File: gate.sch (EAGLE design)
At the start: 25 parts, among them IC1 MAX3232CSE, IC2 LM386M-1, J1 RJ11-2X, X1 MINI-USB-SCHIELD-32005-301

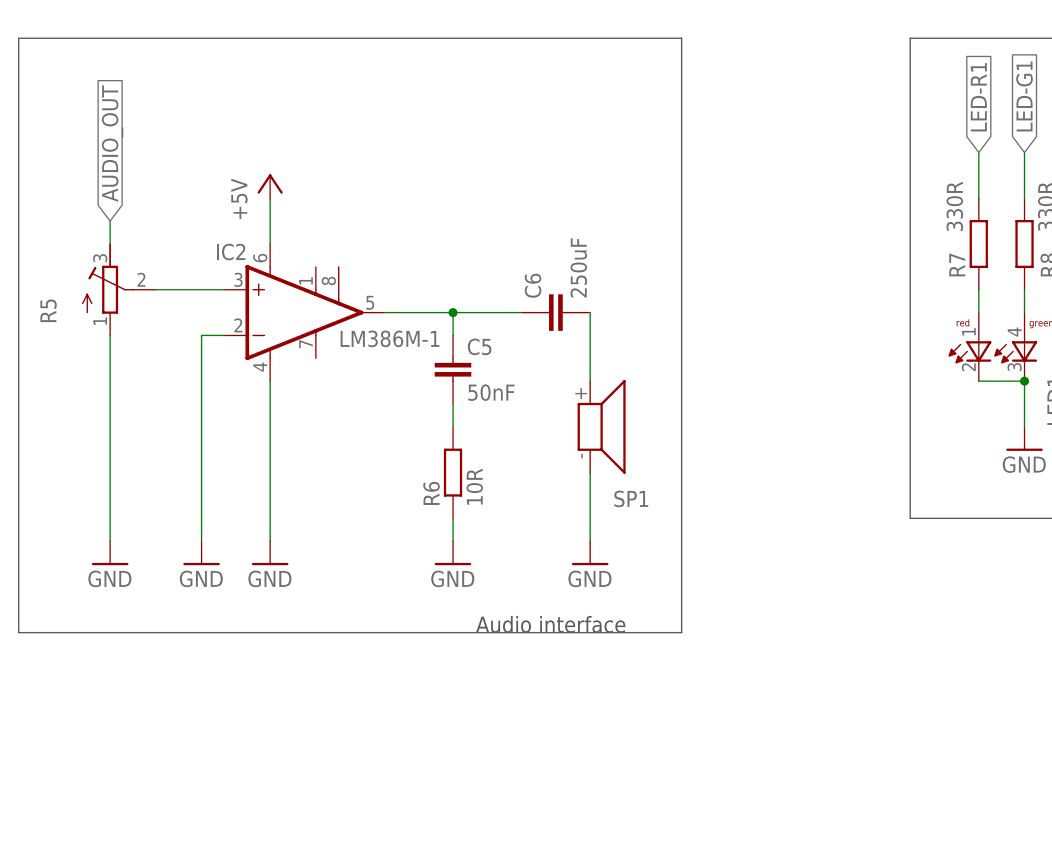
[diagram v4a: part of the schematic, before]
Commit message: Add volume resistor ladder for audio output
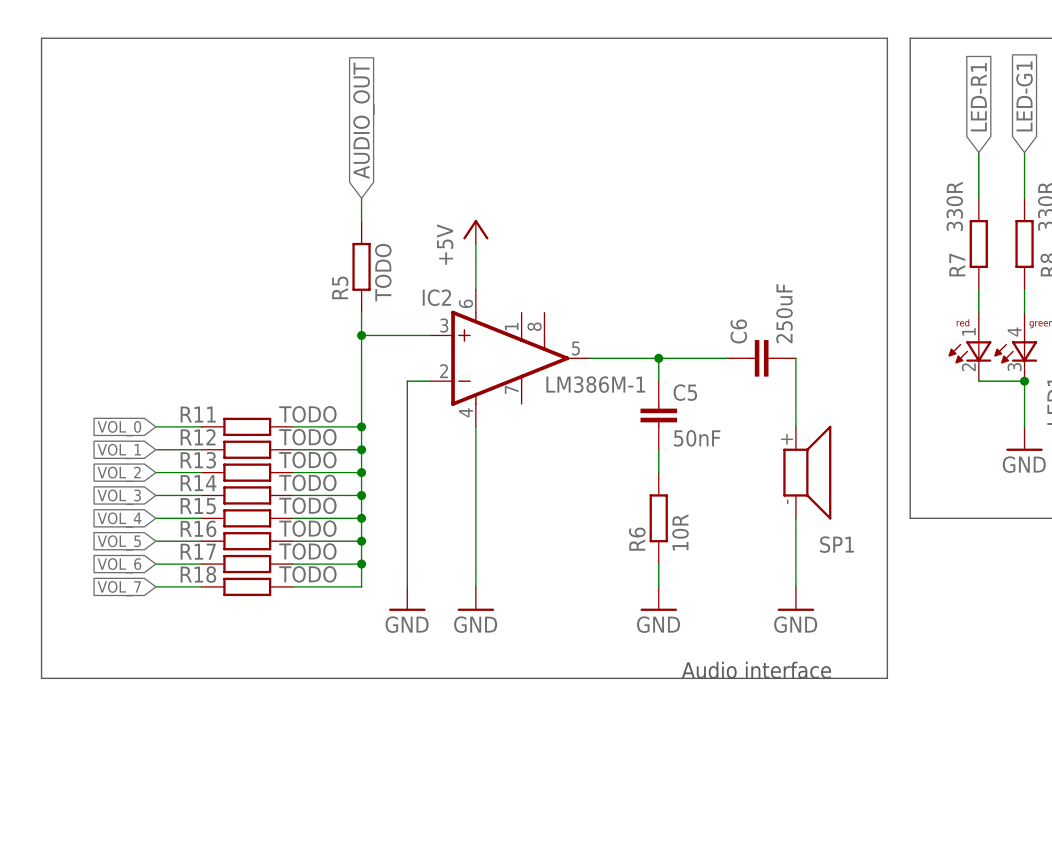
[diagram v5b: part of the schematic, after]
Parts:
- added R11, R12, R13, R14, R15, R16, R17, R18: TODO, rcl:R-EU_R0805
- R5: value (none) -> TODO; device rcl:R-TRIMM3339P -> rcl:R-EU_R0805
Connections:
- new net VOL_0: R11.1
- new net VOL_1: R12.1
- new net VOL_2: R13.1
- new net VOL_3: R14.1
- new net VOL_4: R15.1
- new net VOL_5: R16.1
- new net VOL_6: R17.1
- new net VOL_7: R18.1
- net AUDIO_OUT: now also R5.2; no longer R5.E
- net GND: no longer R5.A
- net N$15: now also R11.2, R12.2, R13.2, R14.2, R15.2, R16.2, R17.2, R18.2, R5.1; no longer R5.S
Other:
- moved on the sheet: C5, C6, IC2, R6, SP1

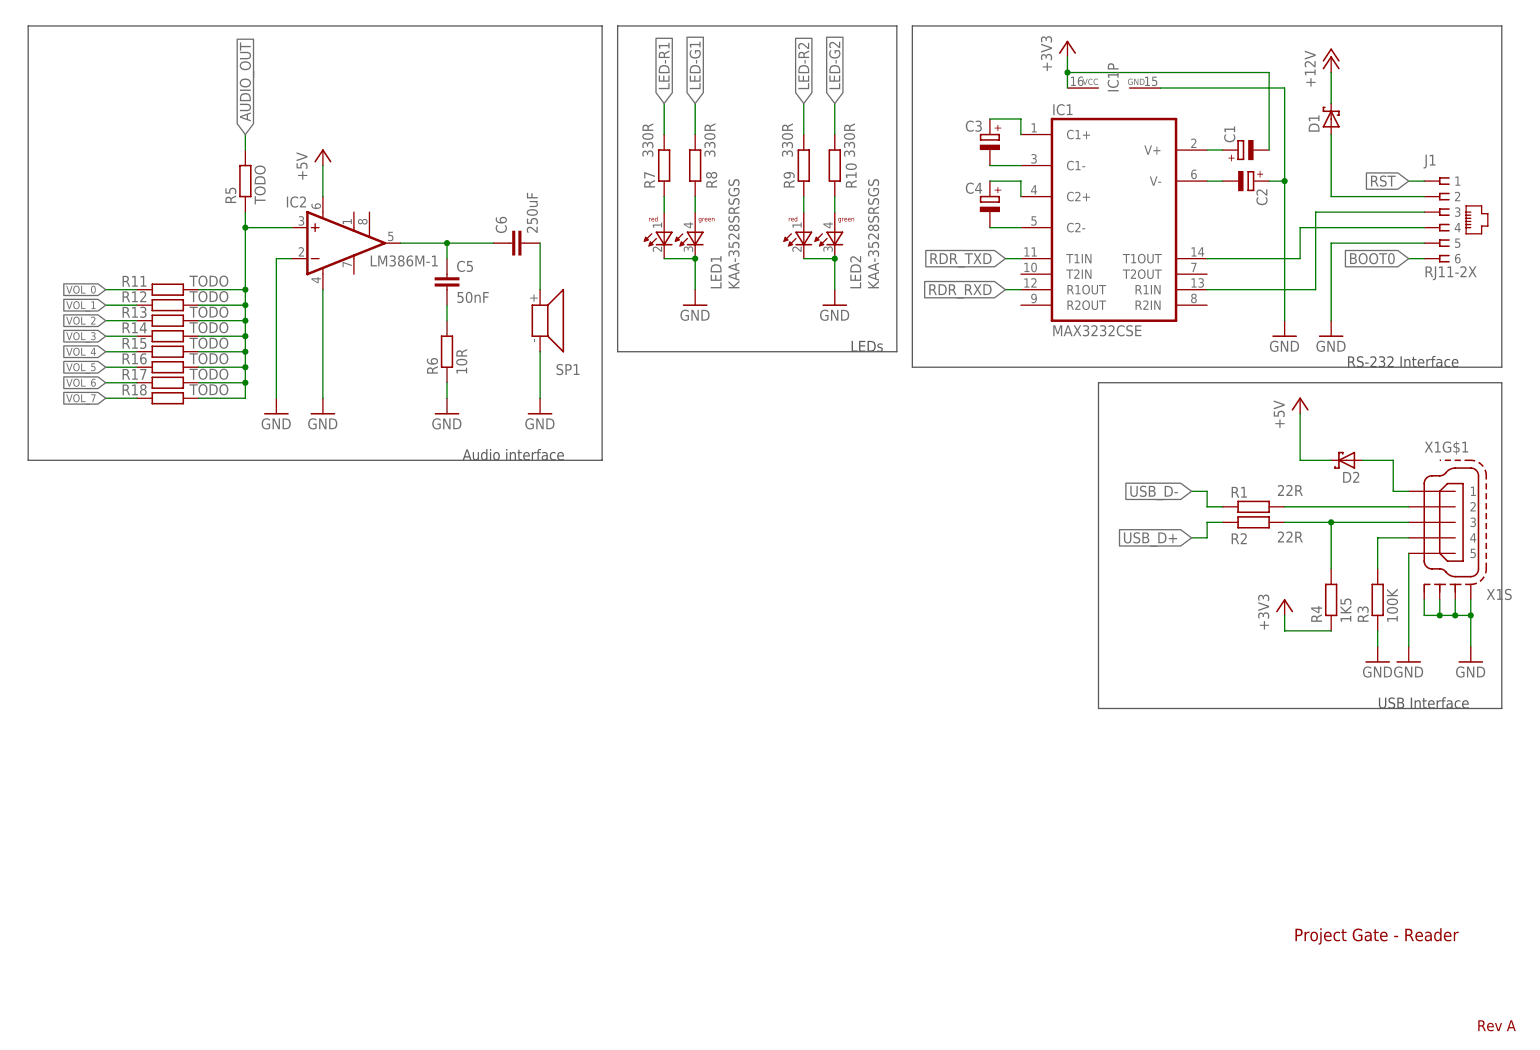
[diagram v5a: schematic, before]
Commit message: Add STM32F0[72|51] MCU
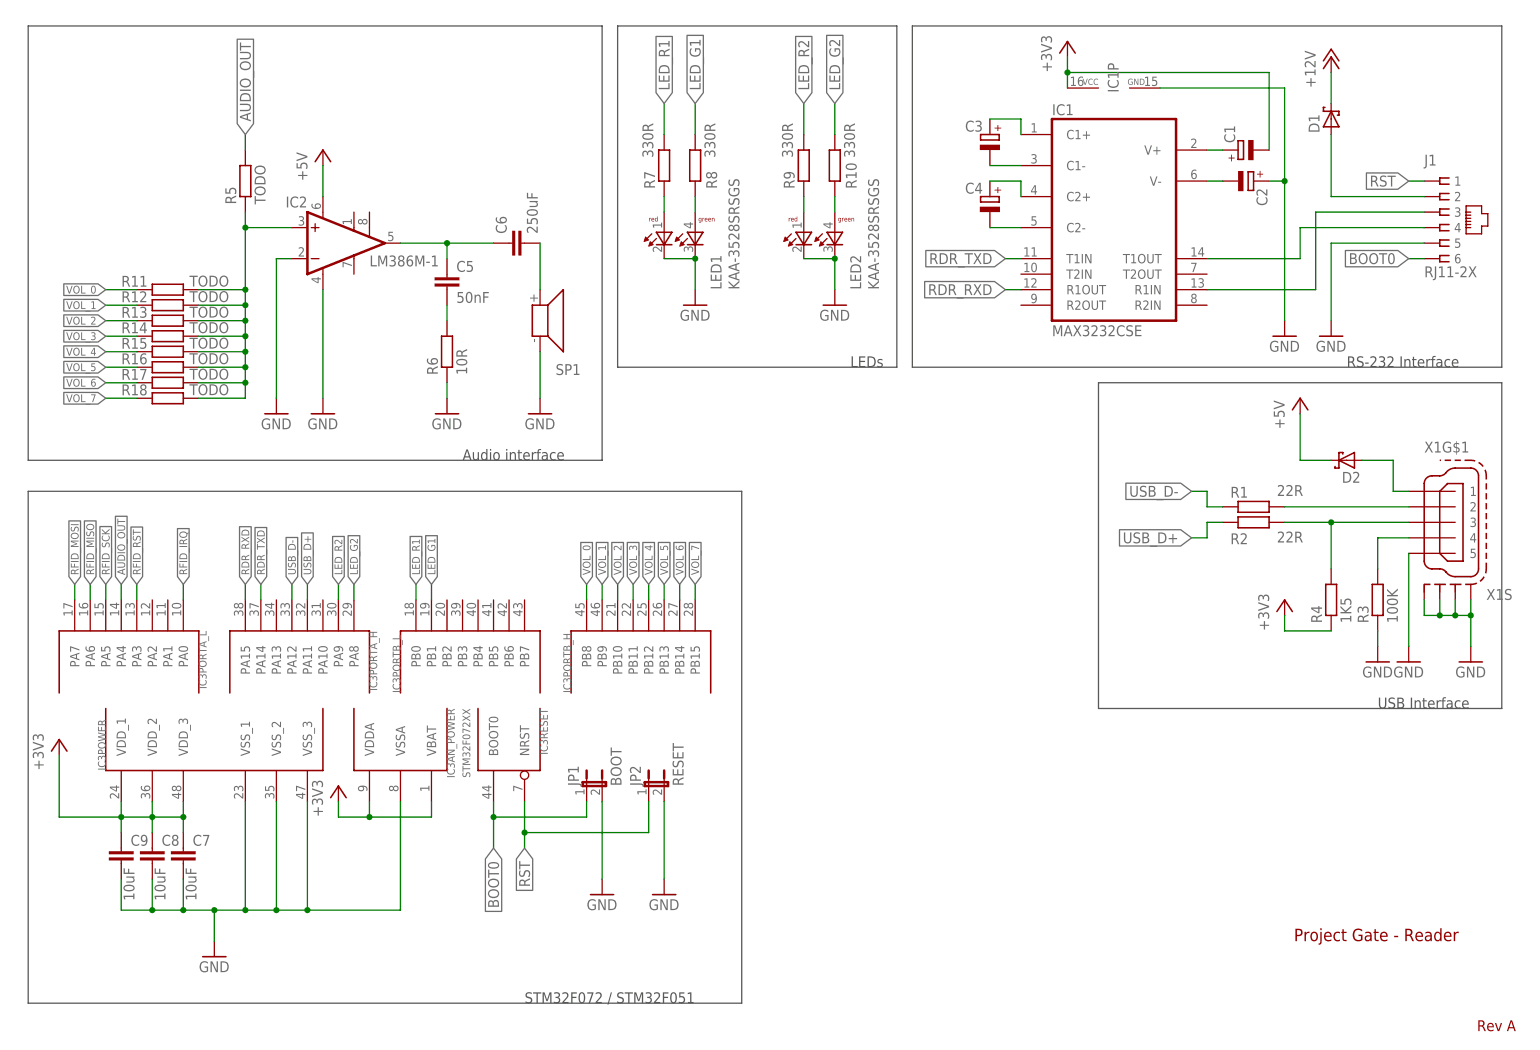
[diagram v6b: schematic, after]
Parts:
- added C7, C8, C9: 10uF, rcl:C-EUC0805
- added IC3: STM32F072XX, stm32f051:STM32F072XX
- added JP1: BOOT, jumper:JP1E
- added JP2: RESET, jumper:JP1E
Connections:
- removed net LED-G1: R8.2
- removed net LED-G2: R10.2
- removed net LED-R1: R7.2
- removed net LED-R2: R9.2
- new net LED_G1: IC3PORTB_L.PB1, R8.2
- new net LED_G2: IC3PORTA_H.PA8, R10.2
- new net LED_R1: IC3PORTB_L.PB0, R7.2
- new net LED_R2: IC3PORTA_H.PA9, R9.2
- new net RFID_IRQ: IC3PORTA_L.PA0
- new net RFID_MISO: IC3PORTA_L.PA6
- new net RFID_MOSI: IC3PORTA_L.PA7
- new net RFID_RST: IC3PORTA_L.PA3
- new net RFID_SCK: IC3PORTA_L.PA5
- net +3V3: now also C7.1, C8.1, C9.1, IC3AN_POWER.VBAT, IC3AN_POWER.VDDA, IC3POWER.VDD_1, IC3POWER.VDD_2, IC3POWER.VDD_3
- net AUDIO_OUT: now also IC3PORTA_L.PA4
- net BOOT0: now also IC3RESET.BOOT0, JP1.1
- net GND: now also C7.2, C8.2, C9.2, IC3AN_POWER.VSSA, IC3POWER.VSS_1, IC3POWER.VSS_2, IC3POWER.VSS_3, JP1.2, JP2.2
- net RDR_RXD: now also IC3PORTA_H.PA15
- net RDR_TXD: now also IC3PORTA_H.PA14
- net RST: now also IC3RESET.NRST, JP2.1
- net USB_D+: now also IC3PORTA_H.PA11
- net USB_D-: now also IC3PORTA_H.PA12
- net VOL_0: now also IC3PORTB_H.PB8
- net VOL_1: now also IC3PORTB_H.PB9
- net VOL_2: now also IC3PORTB_H.PB10
- net VOL_3: now also IC3PORTB_H.PB11
- net VOL_4: now also IC3PORTB_H.PB12
- net VOL_5: now also IC3PORTB_H.PB13
- net VOL_6: now also IC3PORTB_H.PB14
- net VOL_7: now also IC3PORTB_H.PB15
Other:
- note added: "STM32F072 / STM32F051"

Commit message: Add RFID module
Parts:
- added C10: 10uF, rcl:C-EUC0805
- added M1: (no value), mfrc522-module:RFID-RC522
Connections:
- new net RFID_SS: IC3PORTA_L.PA1, M1.8
- net +3V3: now also C10.1, M1.1
- net GND: now also C10.2, M1.3
- net RFID_IRQ: now also M1.4
- net RFID_MISO: now also M1.5
- net RFID_MOSI: now also M1.6
- net RFID_RST: now also M1.2
- net RFID_SCK: now also M1.7
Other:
- note added: "RFID module"
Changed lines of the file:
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@@
 <setting verticaltext="up"/>
 </settings>
-<grid distance="0.1" unitdist="inch" unit="inch" style="lines" multiple="1" display="yes" altdistance="0.01" altunitdist="inch" altunit="inch"/>
+<grid distance="0.05" unitdist="inch" unit="inch" style="lines" multiple="1" display="yes" altdistance="0.01" altunitdist="inch" altunit="inch"/>
 <layers>
 <layer number="1" name="Top" color="4" fill="1" visible="no" active="no"/>
@@
 <part name="+3V3" library="supply1" deviceset="+3V3" device=""/>
 <part name="+3V4" library="supply1" deviceset="+3V3" device=""/>
+<part name="M1" library="mfrc522-module" deviceset="RFID-RC522" device=""/>
+<part name="+3V5" library="supply1" deviceset="+3V3" device=""/>
+<part name="GND15" library="supply1" deviceset="GND" device=""/>
+<part name="C10" library="rcl" deviceset="C-EU" device="C0805" value="10uF"/>
 </parts>
 <sheets>
@@
 <wire x1="10.16" y1="10.16" x2="10.16" y2="93.98" width="0.1524" layer="97"/>
 <text x="91.44" y="10.16" size="1.778" layer="97" font="vector">STM32F072 / STM32F051</text>
+<wire x1="185.42" y1="57.15" x2="251.46" y2="57.15" width="0.1524" layer="97"/>
+<wire x1="251.46" y1="57.15" x2="251.46" y2="26.67" width="0.1524" layer="97"/>
+<wire x1="251.46" y1="26.67" x2="185.42" y2="26.67" width="0.1524" layer="97"/>
+<wire x1="185.42" y1="26.67" x2="185.42" y2="57.15" width="0.1524" layer="97"/>
+<text x="233.68" y="26.67" size="1.778" layer="97" font="vector">RFID module</text>
 </plain>
 <instances>
@@
 <instance part="+3V3" gate="G$1" x="15.24" y="53.34"/>
 <instance part="+3V4" gate="G$1" x="60.96" y="45.72"/>
+<instance part="M1" gate="A" x="227.33" y="43.18" smashed="yes">
+<attribute name="NAME" x="243.84" y="51.435" size="1.778" layer="95"/>
+<attribute name="VALUE" x="223.52" y="27.94" size="1.778" layer="96"/>
+</instance>
+<instance part="+3V5" gate="G$1" x="198.12" y="55.88" smashed="yes">
+<attribute name="VALUE" x="199.39" y="54.61" size="1.778" layer="96"/>
+</instance>
+<instance part="GND15" gate="1" x="198.12" y="30.48"/>
+<instance part="C10" gate="G$1" x="195.58" y="49.53" smashed="yes">
+<attribute name="NAME" x="194.564" y="51.181" size="1.778" layer="95" rot="R180"/>
+<attribute name="VALUE" x="194.945" y="41.656" size="1.778" layer="96" rot="R90"/>
+</instance>
 </instances>
 <busses>
@@
 <junction x="55.88" y="25.4"/>
 </segment>
+<segment>
+<pinref part="M1" gate="A" pin="3"/>
+<pinref part="GND15" gate="1" pin="GND"/>
+<wire x1="224.79" y1="46.99" x2="198.12" y2="46.99" width="0.1524" layer="91"/>
+<wire x1="198.12" y1="46.99" x2="198.12" y2="44.45" width="0.1524" layer="91"/>
+<pinref part="C10" gate="G$1" pin="2"/>
+<wire x1="198.12" y1="44.45" x2="198.12" y2="33.02" width="0.1524" layer="91"/>
+<wire x1="195.58" y1="44.45" x2="198.12" y2="44.45" width="0.1524" layer="91"/>
+<junction x="198.12" y="44.45"/>
+</segment>
 </net>
 <net name="N$1" class="0">
@@
 <wire x1="76.2" y1="40.64" x2="66.04" y2="40.64" width="0.1524" layer="91"/>
 <junction x="66.04" y="40.64"/>
+</segment>
+<segment>
+<pinref part="M1" gate="A" pin="1"/>
+<pinref part="+3V5" gate="G$1" pin="+3V3"/>
+<wire x1="224.79" y1="52.07" x2="198.12" y2="52.07" width="0.1524" layer="91"/>
+<wire x1="198.12" y1="52.07" x2="198.12" y2="53.34" width="0.1524" layer="91"/>
+<pinref part="C10" gate="G$1" pin="1"/>
+<wire x1="195.58" y1="52.07" x2="198.12" y2="52.07" width="0.1524" layer="91"/>
+<junction x="198.12" y="52.07"/>
 </segment>
 </net>
@@
 <label x="22.86" y="78.74" size="1.27" layer="95" rot="R90" xref="yes"/>
 </segment>
+<segment>
+<pinref part="M1" gate="A" pin="7"/>
+<wire x1="224.79" y1="36.83" x2="214.63" y2="36.83" width="0.1524" layer="91"/>
+<label x="214.63" y="36.83" size="1.27" layer="95" rot="R180" xref="yes"/>
+</segment>
 </net>
 <net name="RFID_MISO" class="0">
@@
 <label x="20.32" y="78.74" size="1.27" layer="95" rot="R90" xref="yes"/>
 </segment>
+<segment>
+<pinref part="M1" gate="A" pin="5"/>
+<wire x1="224.79" y1="41.91" x2="214.63" y2="41.91" width="0.1524" layer="91"/>
+<label x="214.63" y="41.91" size="1.27" layer="95" rot="R180" xref="yes"/>
+</segment>
 </net>
 <net name="RFID_MOSI" class="0">
@@
 <label x="17.78" y="78.74" size="1.27" layer="95" rot="R90" xref="yes"/>
 </segment>
+<segment>
+<pinref part="M1" gate="A" pin="6"/>
+<wire x1="224.79" y1="39.37" x2="214.63" y2="39.37" width="0.1524" layer="91"/>
+<label x="214.63" y="39.37" size="1.27" layer="95" rot="R180" xref="yes"/>
+</segment>
 </net>
 <net name="RFID_RST" class="0">
@@
 <label x="27.94" y="78.74" size="1.27" layer="95" rot="R90" xref="yes"/>
 </segment>
+<segment>
+<pinref part="M1" gate="A" pin="2"/>
+<wire x1="224.79" y1="49.53" x2="214.63" y2="49.53" width="0.1524" layer="91"/>
+<label x="214.63" y="49.53" size="1.27" layer="95" rot="R180" xref="yes"/>
+</segment>
 </net>
 <net name="RFID_IRQ" class="0">
@@
 <label x="35.56" y="78.74" size="1.27" layer="95" rot="R90" xref="yes"/>
 </segment>
+<segment>
+<pinref part="M1" gate="A" pin="4"/>
+<wire x1="224.79" y1="44.45" x2="214.63" y2="44.45" width="0.1524" layer="91"/>
+<label x="214.63" y="44.45" size="1.27" layer="95" rot="R180" xref="yes"/>
+</segment>
 </net>
 <net name="LED_G2" class="0">
@@
 </segment>
 </net>
+<net name="RFID_SS" class="0">
+<segment>
+<pinref part="IC3" gate="PORTA_L" pin="PA1"/>
+<wire x1="33.02" y1="76.2" x2="33.02" y2="78.74" width="0.1524" layer="91"/>
+<label x="33.02" y="78.74" size="1.27" layer="95" rot="R90" xref="yes"/>
+</segment>
+<segment>
+<pinref part="M1" gate="A" pin="8"/>
+<wire x1="224.79" y1="34.29" x2="214.63" y2="34.29" width="0.1524" layer="91"/>
+<label x="214.63" y="34.29" size="1.27" layer="95" rot="R180" xref="yes"/>
+</segment>
+</net>

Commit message: Add SWD header
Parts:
- added JP3: (no value), pinhead:PINHD-1X6
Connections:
- removed net RDR_TXD: IC1G$1.T1IN, IC3PORTA_H.PA14
- new net RDR_TXD/SWDIO: IC1G$1.T1IN, IC3PORTA_H.PA14, JP3.4
- new net SWCLK: IC3PORTA_H.PA13, JP3.2
- new net T_SWO: IC3PORTB_L.PB3, JP3.6
- net +3V3: now also JP3.1
- net GND: now also JP3.3
- net RST: now also JP3.5
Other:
- note added: "SWD"
- moved on the sheet: C1, C2, C3, C4, D1, IC1, IC1P
